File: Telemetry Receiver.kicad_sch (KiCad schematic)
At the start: 29 parts, among them J2 USB_A, J3 S4B-XH-A-1, U1 LM1117-3.3, U2 USBLC6-2SC6, U3 STM32L4P5RET6, U5 36103205S, Y2 Crystal(32.756MHz)

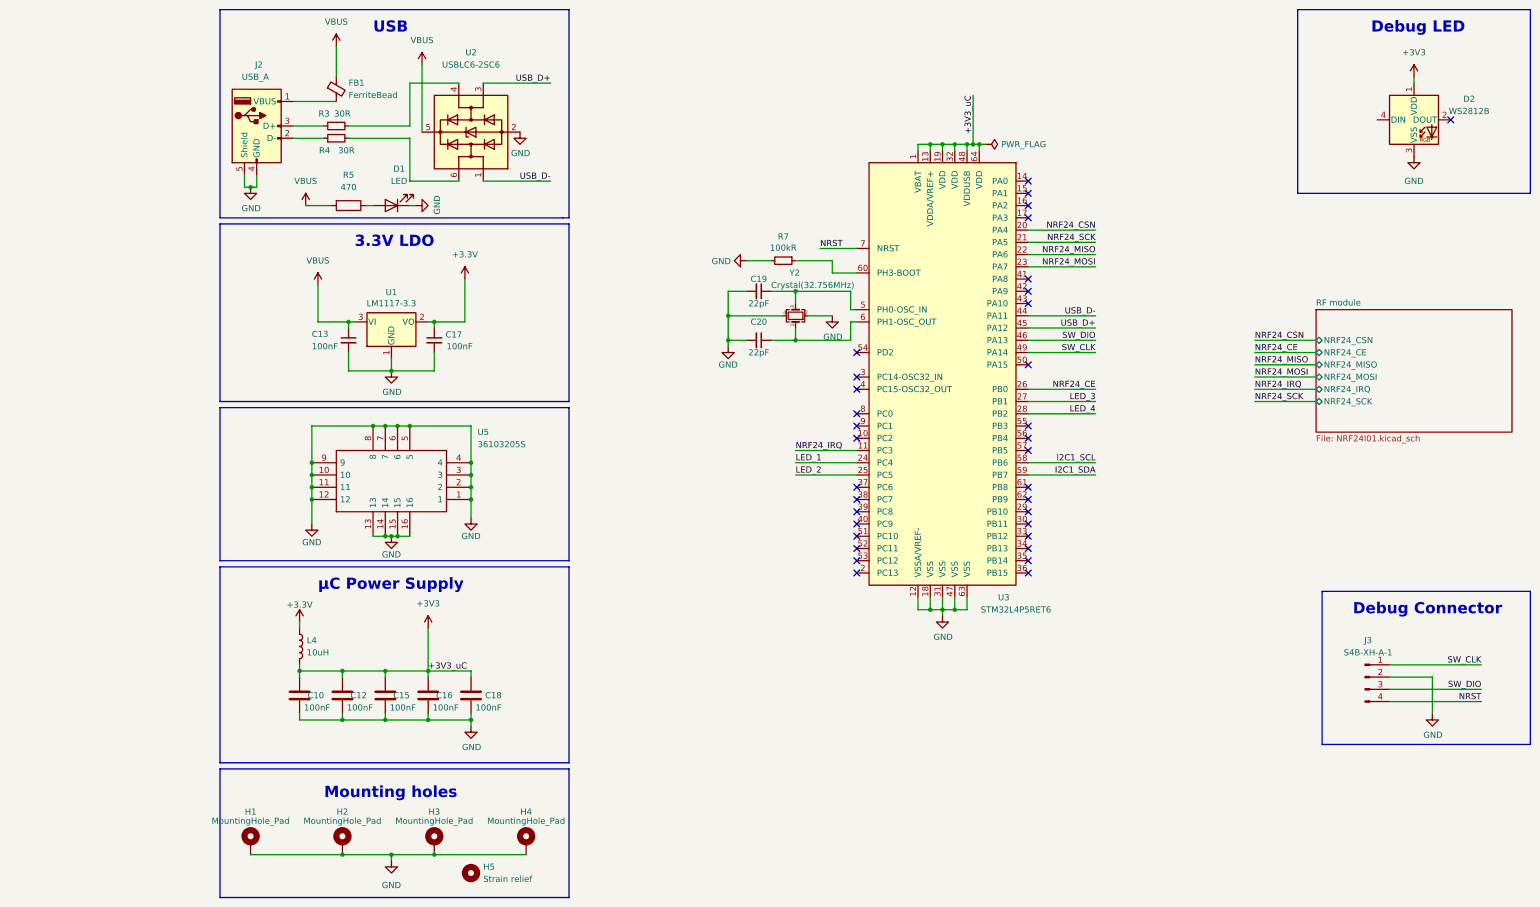
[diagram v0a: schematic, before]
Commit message: Changed goldpin connector to micro usb
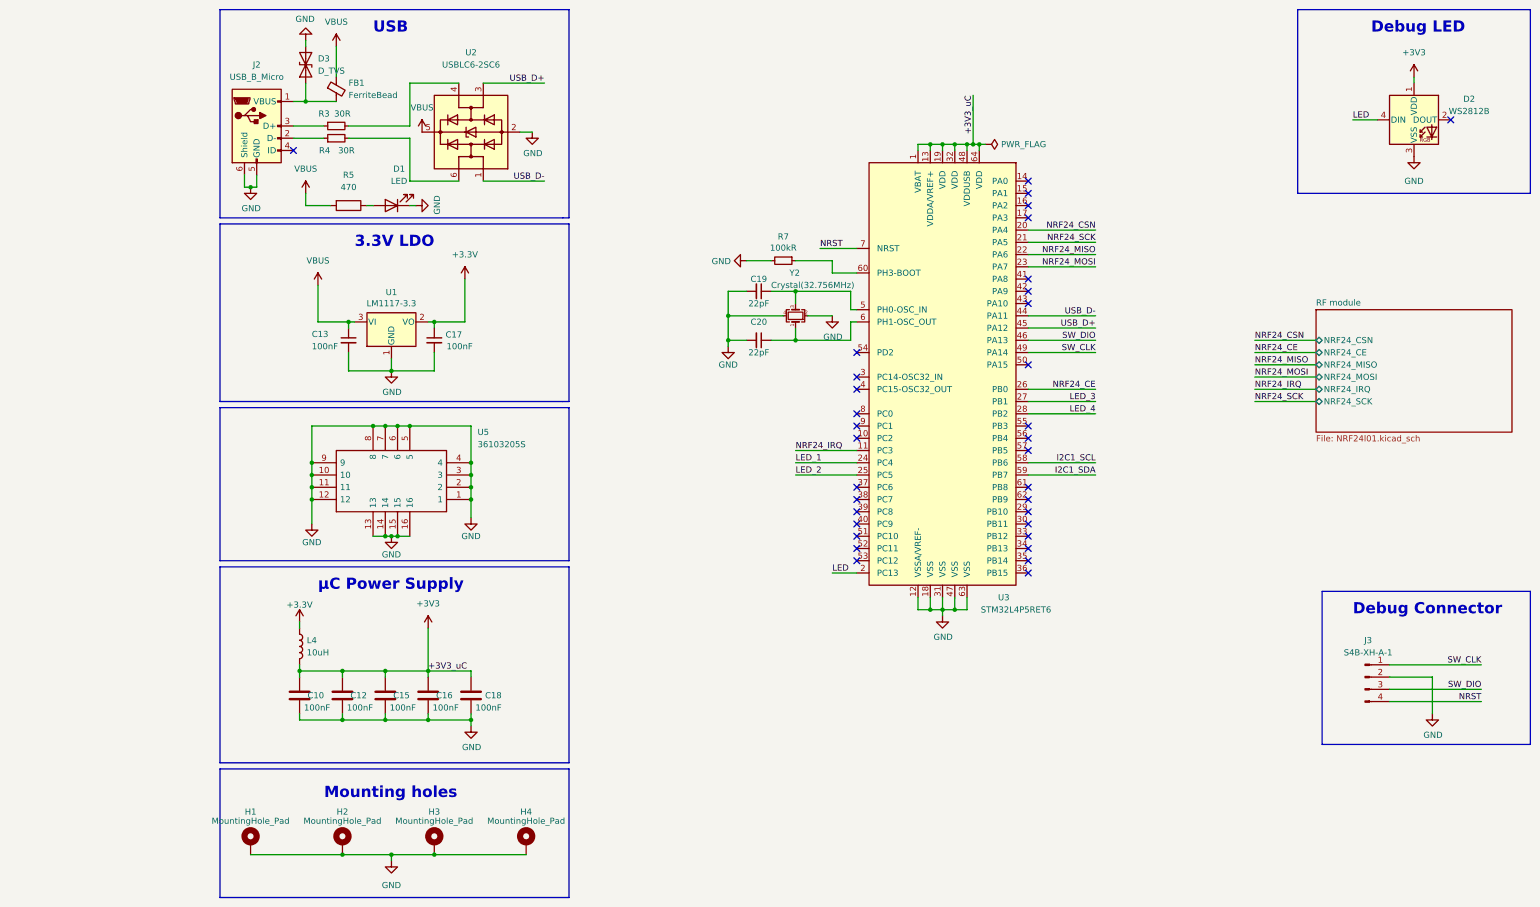
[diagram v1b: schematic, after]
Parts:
- removed H5: Strain relief, MountingHole:MountingHole_3.2mm_M3_DIN965, symbol Mechanical:MountingHole
- removed J2: USB_A, Connector_PinHeader_1.27mm:PinHeader_1x04_P1.27mm_Vertical, symbol Connector:USB_A
- added D3: D_TVS, Diode_SMD:D_0402_1005Metric, symbol Device:D_TVS
- added J2: USB_B_Micro, Connector_USB:USB_Micro-B_Molex_47346-0001, symbol Connector:USB_B_Micro
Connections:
- net GND: now also D3.2 (A2), J2.5 (GND), J2.6 (Shield)
- net at FB1.2: now also D3.1 (A1), J2.1 (VBUS)
- net LED: now reaches D2.4 (DIN)
- net LED: now also U3.2 (PC13)
- net at R3.1: now also J2.3 (D+)
- net at R4.1: now also J2.2 (D-)

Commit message: 4 layer PCB
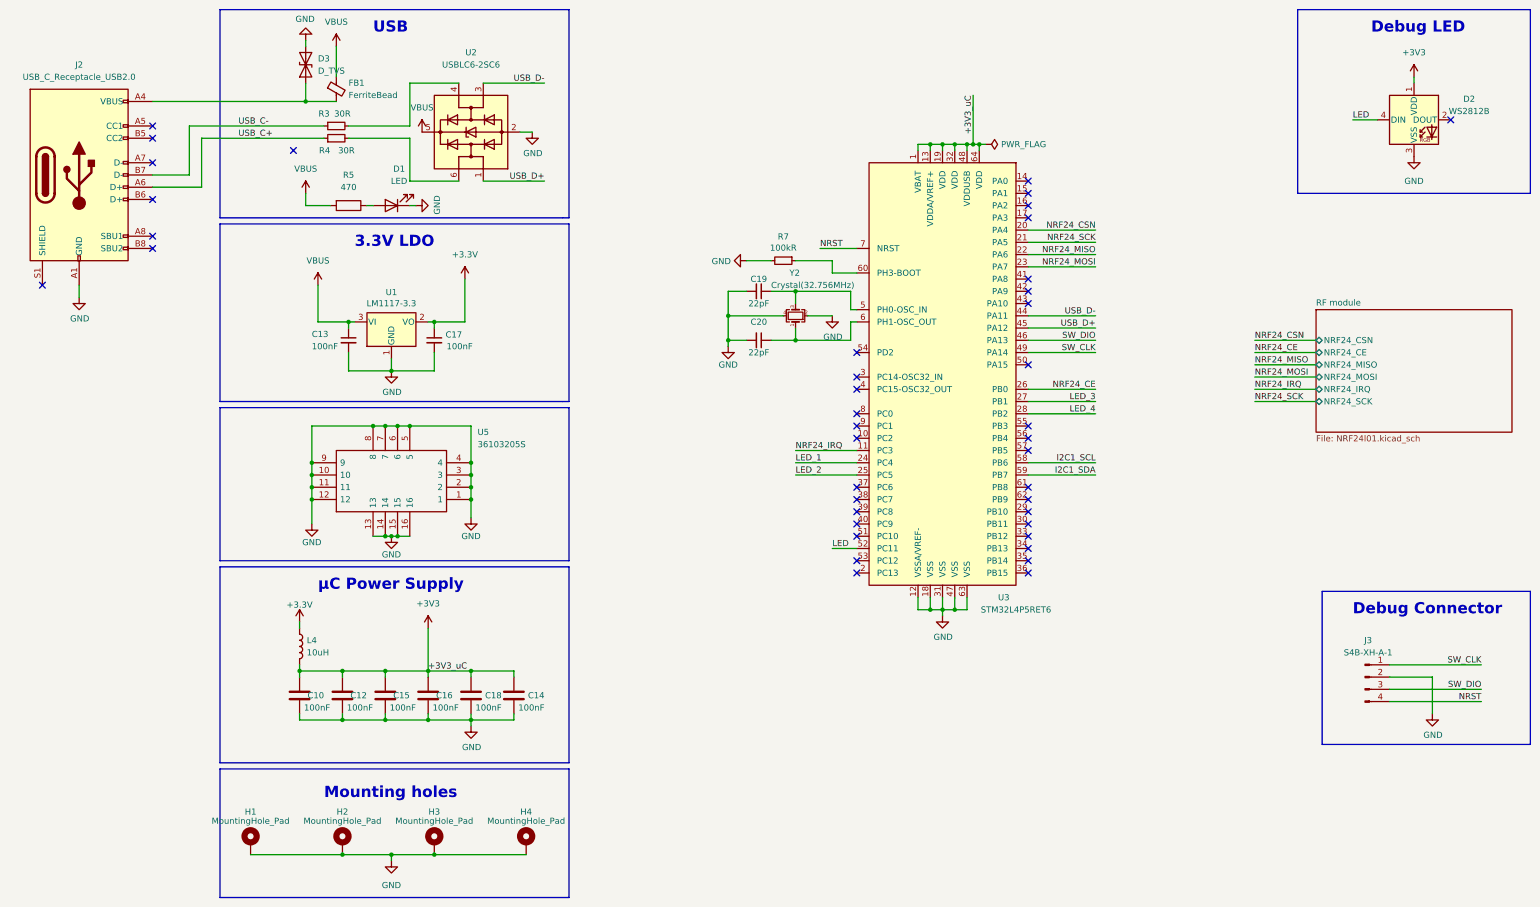
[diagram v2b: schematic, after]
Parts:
- removed J2: USB_B_Micro, Connector_USB:USB_Micro-B_Molex_47346-0001, symbol Connector:USB_B_Micro
- added C14: 100nF, Capacitor_SMD:C_0402_1005Metric, symbol Device:C
- added J2: USB_C_Receptacle_USB2.0, Connector_USB:USB_C_Receptacle_HRO_TYPE-C-31-M-12, symbol Connector:USB_C_Receptacle_USB2.0
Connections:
- net +3V3: now also C14.1
- net GND: now also C14.2, J2.A1 (GND), J2.A12 (GND), J2.B1 (GND), J2.B12 (GND)
- net LED: now also U3.52 (PC11); no longer U3.2 (PC13)
- net USB_D+: now also U2.1 (I/O1); no longer U2.3 (I/O2)
- net USB_D-: now also U2.3 (I/O2); no longer U2.1 (I/O1)
- net at D3.1 (A1), FB1.2: now also J2.A4 (VBUS), J2.A9 (VBUS), J2.B4 (VBUS), J2.B9 (VBUS)
- net USB_C+: now reaches R4.1
- net USB_C+: now also J2.A6 (D+)
- net USB_C-: now reaches R3.1
- net USB_C-: now also J2.B7 (D-)
- no-connect marks 34 -> 41

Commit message: New 3d models
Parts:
- H1, H2, H3, H4: footprint MountingHole:MountingHole_2.2mm_M2_DIN965_Pad_TopBottom -> MountingHole:MountingHole_3.2mm_M3_DIN965_Pad
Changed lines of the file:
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@@
     (property "Reference" "H1" (id 0) (at 19.05 179.07 0))
     (property "Value" "MountingHole_Pad" (id 1) (at 19.05 180.975 0))
-    (property "Footprint" "MountingHole:MountingHole_2.2mm_M2_DIN965_Pad_TopBottom" (id 2) (at 19.05 185.42 0)
+    (property "Footprint" "MountingHole:MountingHole_3.2mm_M3_DIN965_Pad" (id 2) (at 19.05 185.42 0)
       (effects (font (size 1.27 1.27)) hide)
     )
@@
     (property "Reference" "H3" (id 0) (at 57.15 179.07 0))
     (property "Value" "MountingHole_Pad" (id 1) (at 57.15 180.975 0))
-    (property "Footprint" "MountingHole:MountingHole_2.2mm_M2_DIN965_Pad_TopBottom" (id 2) (at 57.15 185.42 0)
+    (property "Footprint" "MountingHole:MountingHole_3.2mm_M3_DIN965_Pad" (id 2) (at 57.15 185.42 0)
       (effects (font (size 1.27 1.27)) hide)
     )
@@
     (property "Reference" "H2" (id 0) (at 38.1 179.07 0))
     (property "Value" "MountingHole_Pad" (id 1) (at 38.1 180.975 0))
-    (property "Footprint" "MountingHole:MountingHole_2.2mm_M2_DIN965_Pad_TopBottom" (id 2) (at 38.1 185.42 0)
+    (property "Footprint" "MountingHole:MountingHole_3.2mm_M3_DIN965_Pad" (id 2) (at 38.1 185.42 0)
       (effects (font (size 1.27 1.27)) hide)
     )
@@
     (property "Reference" "H4" (id 0) (at 76.2 179.07 0))
     (property "Value" "MountingHole_Pad" (id 1) (at 76.2 180.975 0))
-    (property "Footprint" "MountingHole:MountingHole_2.2mm_M2_DIN965_Pad_TopBottom" (id 2) (at 76.2 185.42 0)
+    (property "Footprint" "MountingHole:MountingHole_3.2mm_M3_DIN965_Pad" (id 2) (at 76.2 185.42 0)
       (effects (font (size 1.27 1.27)) hide)
     )
@@
     )
     (path "/a340fb87-fb6f-4872-8325-c076714bac15"
-      (reference "H1") (unit 1) (value "MountingHole_Pad") (footprint "MountingHole:MountingHole_2.2mm_M2_DIN965_Pad_TopBottom")
+      (reference "H1") (unit 1) (value "MountingHole_Pad") (footprint "MountingHole:MountingHole_3.2mm_M3_DIN965_Pad")
     )
     (path "/ca7df565-b491-47af-b824-b4827cdfc16c"
-      (reference "H2") (unit 1) (value "MountingHole_Pad") (footprint "MountingHole:MountingHole_2.2mm_M2_DIN965_Pad_TopBottom")
+      (reference "H2") (unit 1) (value "MountingHole_Pad") (footprint "MountingHole:MountingHole_3.2mm_M3_DIN965_Pad")
     )
     (path "/c6ad2c0c-b21f-44b7-8751-6190f5eca7a7"
-      (reference "H3") (unit 1) (value "MountingHole_Pad") (footprint "MountingHole:MountingHole_2.2mm_M2_DIN965_Pad_TopBottom")
+      (reference "H3") (unit 1) (value "MountingHole_Pad") (footprint "MountingHole:MountingHole_3.2mm_M3_DIN965_Pad")
     )
     (path "/f5d8f318-dec3-4171-9cff-179b5c9019d9"
-      (reference "H4") (unit 1) (value "MountingHole_Pad") (footprint "MountingHole:MountingHole_2.2mm_M2_DIN965_Pad_TopBottom")
+      (reference "H4") (unit 1) (value "MountingHole_Pad") (footprint "MountingHole:MountingHole_3.2mm_M3_DIN965_Pad")
     )
     (path "/85926aab-78d2-4086-959c-d3cde54f1743/20bdb3f5-9684-4690-b2a1-8872c1e28dcb"
